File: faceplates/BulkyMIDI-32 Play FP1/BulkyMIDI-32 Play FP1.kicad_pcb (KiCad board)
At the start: 2 copper layers, 100 x 23.2 mm, 4 parts, among them M1 Mounting_Pin, M2 Mounting_Pin, M3 Mounting_Pin, M4 Mounting_Pin

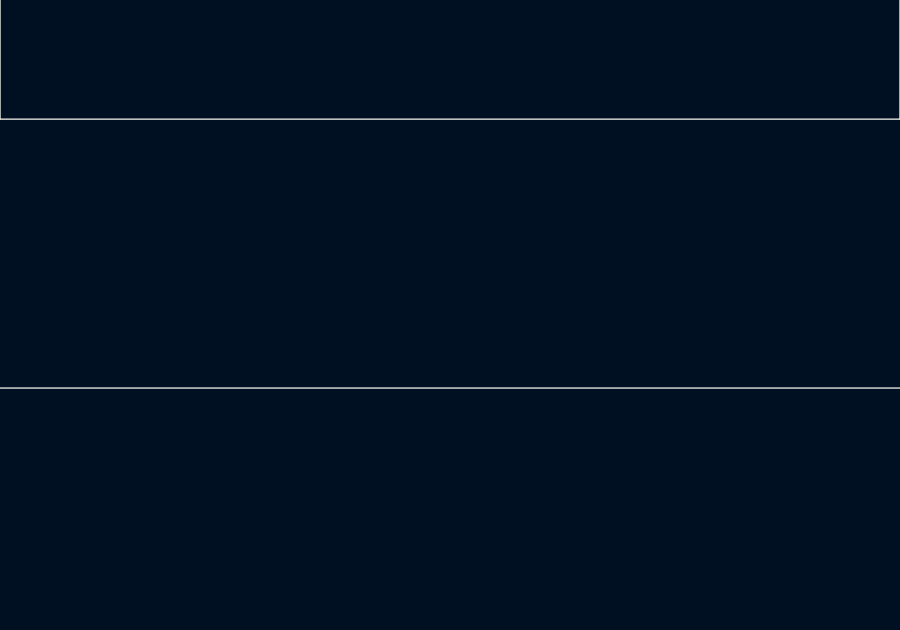
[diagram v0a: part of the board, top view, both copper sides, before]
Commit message: Channel logo added to FP1, same with Play
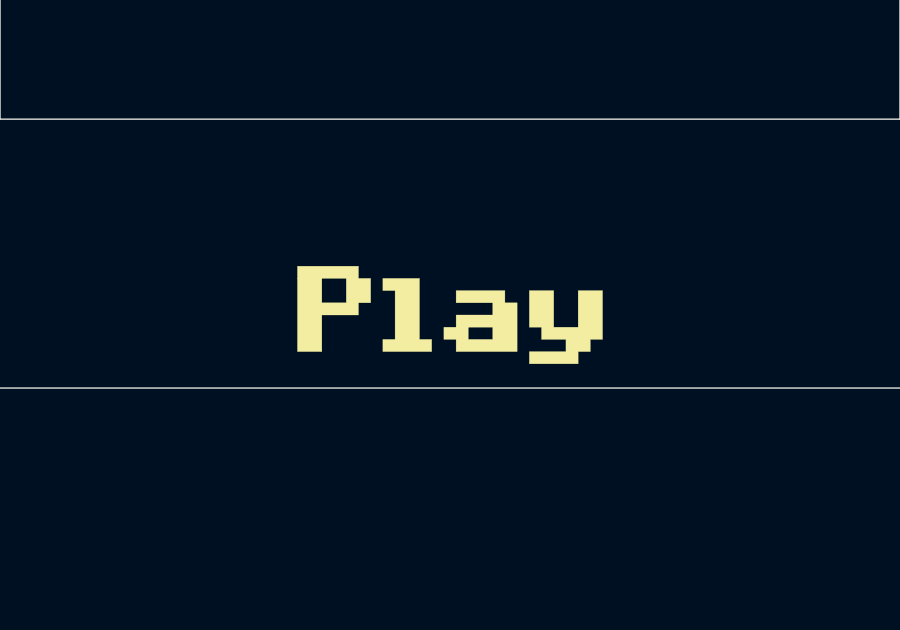
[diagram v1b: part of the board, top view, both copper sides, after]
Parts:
- added G***: LOGO, artwork:Play, F.Cu at (141.1, 131.7)
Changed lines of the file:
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@@
     (tracks 0)
     (zones 0)
-    (modules 4)
+    (modules 5)
     (nets 2)
   )
@@
     (add_net GND)
   )
+  (module artwork:Play (layer F.Cu)
+    (at 141.09 131.739)
+    (fp_text reference G*** (at 0 0) (layer F.SilkS) hide
+      (effects (font (size 1.524 1.524) (thickness 0.3)))
+    )
+    (fp_text value LOGO (at 0.75 0) (layer F.SilkS) hide
+      (effects (font (size 1.524 1.524) (thickness 0.3)))
+    )
+    (fp_poly (pts (xy 3.457857 0.406807) (xy 4.271471 0.406807) (xy 4.271471 -0.813614) (xy 5.085085 -0.813614)
+      (xy 5.085085 0.813613) (xy 4.678278 0.813613) (xy 4.678278 1.22042) (xy 4.271471 1.22042)
+      (xy 4.271471 1.627227) (xy 2.644244 1.627227) (xy 2.644244 1.22042) (xy 3.864664 1.22042)
+      (xy 3.864664 0.813613) (xy 3.051051 0.813613) (xy 3.051051 0.406807) (xy 2.644244 0.406807)
+      (xy 2.644244 -0.813614) (xy 3.457857 -0.813614) (xy 3.457857 0.406807)) (layer F.SilkS) (width 0.01))
+    (fp_poly (pts (xy -3.051051 -1.220421) (xy -2.644245 -1.220421) (xy -2.644245 -0.406807) (xy -3.051051 -0.406807)
+      (xy -3.051051 0) (xy -4.271472 0) (xy -4.271472 1.22042) (xy -5.085085 1.22042)
+      (xy -5.085085 -1.220421) (xy -4.271472 -1.220421) (xy -4.271472 -0.406807) (xy -3.457858 -0.406807)
+      (xy -3.457858 -1.220421) (xy -4.271472 -1.220421) (xy -5.085085 -1.220421) (xy -5.085085 -1.627227)
+      (xy -3.051051 -1.627227) (xy -3.051051 -1.220421)) (layer F.SilkS) (width 0.01))
+    (fp_poly (pts (xy -1.017017 0.813613) (xy -0.610211 0.813613) (xy -0.610211 1.22042) (xy -2.237438 1.22042)
+      (xy -2.237438 0.813613) (xy -1.830631 0.813613) (xy -1.830631 -0.813614) (xy -2.237438 -0.813614)
+      (xy -2.237438 -1.220421) (xy -1.017017 -1.220421) (xy -1.017017 0.813613)) (layer F.SilkS) (width 0.01))
+    (fp_poly (pts (xy 1.83063 -0.406807) (xy 2.237437 -0.406807) (xy 2.237437 1.22042) (xy 0.203403 1.22042)
+      (xy 0.203403 0.813613) (xy -0.203404 0.813613) (xy -0.203404 0.406807) (xy 0.203403 0.406807)
+      (xy 0.61021 0.406807) (xy 0.61021 0.813613) (xy 1.423823 0.813613) (xy 1.423823 0.406807)
+      (xy 0.61021 0.406807) (xy 0.203403 0.406807) (xy 0.203403 0) (xy 1.423823 0)
+      (xy 1.423823 -0.406807) (xy 0.203403 -0.406807) (xy 0.203403 -0.813614) (xy 1.83063 -0.813614)
+      (xy 1.83063 -0.406807)) (layer F.SilkS) (width 0.01))
+  )
   (module mounting:M3_pin (layer F.Cu)
     (at 99.815 129.199)
@@
       (effects (font (size 1 1) (thickness 0.15)))
     )
+    (fp_circle (center 0 0) (end 2 0.8) (layer F.Fab) (width 0.1))
     (fp_circle (center 0 0) (end 2.6 0) (layer F.CrtYd) (width 0.05))
-    (fp_circle (center 0 0) (end 2 0.8) (layer F.Fab) (width 0.1))
     (pad 1 thru_hole circle (at 0 0) (size 3.5 3.5) (drill 3.048) (layers *.Cu *.Mask)
       (net 1 GND) (solder_mask_margin 0.8))
@@
       (effects (font (size 1 1) (thickness 0.15)))
     )
+    (fp_circle (center 0 0) (end 2.6 0) (layer F.CrtYd) (width 0.05))
     (fp_circle (center 0 0) (end 2 0.8) (layer F.Fab) (width 0.1))
-    (fp_circle (center 0 0) (end 2.6 0) (layer F.CrtYd) (width 0.05))
     (pad 1 thru_hole circle (at 0 0) (size 3.5 3.5) (drill 3.048) (layers *.Cu *.Mask)
       (net 1 GND) (solder_mask_margin 0.8))
@@
       (effects (font (size 1 1) (thickness 0.15)))
     )
+    (fp_circle (center 0 0) (end 2 0.8) (layer F.Fab) (width 0.1))
     (fp_circle (center 0 0) (end 2.6 0) (layer F.CrtYd) (width 0.05))
-    (fp_circle (center 0 0) (end 2 0.8) (layer F.Fab) (width 0.1))
     (pad 1 thru_hole circle (at 0 0) (size 3.5 3.5) (drill 3.048) (layers *.Cu *.Mask)
       (net 1 GND) (solder_mask_margin 0.8))
@@
       (effects (font (size 1 1) (thickness 0.15)))
     )
+    (fp_circle (center 0 0) (end 2.6 0) (layer F.CrtYd) (width 0.05))
     (fp_circle (center 0 0) (end 2 0.8) (layer F.Fab) (width 0.1))
-    (fp_circle (center 0 0) (end 2.6 0) (layer F.CrtYd) (width 0.05))
     (pad 1 thru_hole circle (at 0 0) (size 3.5 3.5) (drill 3.048) (layers *.Cu *.Mask)
       (net 1 GND) (solder_mask_margin 0.8))

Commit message: Silkscreen logo tweak
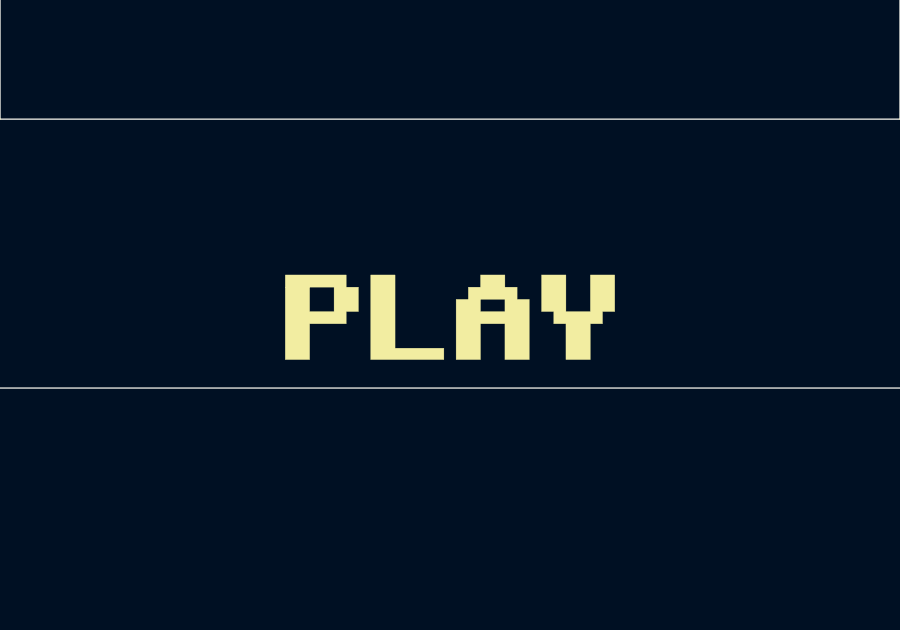
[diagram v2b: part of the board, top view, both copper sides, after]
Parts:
- moved G*** 0.06 mm to (141.1, 131.8)
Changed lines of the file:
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@@
     (add_net GND)
   )
-  (module artwork:Play (layer F.Cu)
-    (at 141.09 131.739)
+  (module artwork:Play locked (layer F.Cu)
+    (at 141.09 131.8025)
     (fp_text reference G*** (at 0 0) (layer F.SilkS) hide
       (effects (font (size 1.524 1.524) (thickness 0.3)))
@@
       (effects (font (size 1.524 1.524) (thickness 0.3)))
     )
-    (fp_poly (pts (xy 3.457857 0.406807) (xy 4.271471 0.406807) (xy 4.271471 -0.813614) (xy 5.085085 -0.813614)
-      (xy 5.085085 0.813613) (xy 4.678278 0.813613) (xy 4.678278 1.22042) (xy 4.271471 1.22042)
-      (xy 4.271471 1.627227) (xy 2.644244 1.627227) (xy 2.644244 1.22042) (xy 3.864664 1.22042)
-      (xy 3.864664 0.813613) (xy 3.051051 0.813613) (xy 3.051051 0.406807) (xy 2.644244 0.406807)
-      (xy 2.644244 -0.813614) (xy 3.457857 -0.813614) (xy 3.457857 0.406807)) (layer F.SilkS) (width 0.01))
-    (fp_poly (pts (xy -3.051051 -1.220421) (xy -2.644245 -1.220421) (xy -2.644245 -0.406807) (xy -3.051051 -0.406807)
-      (xy -3.051051 0) (xy -4.271472 0) (xy -4.271472 1.22042) (xy -5.085085 1.22042)
-      (xy -5.085085 -1.220421) (xy -4.271472 -1.220421) (xy -4.271472 -0.406807) (xy -3.457858 -0.406807)
-      (xy -3.457858 -1.220421) (xy -4.271472 -1.220421) (xy -5.085085 -1.220421) (xy -5.085085 -1.627227)
-      (xy -3.051051 -1.627227) (xy -3.051051 -1.220421)) (layer F.SilkS) (width 0.01))
-    (fp_poly (pts (xy -1.017017 0.813613) (xy -0.610211 0.813613) (xy -0.610211 1.22042) (xy -2.237438 1.22042)
-      (xy -2.237438 0.813613) (xy -1.830631 0.813613) (xy -1.830631 -0.813614) (xy -2.237438 -0.813614)
-      (xy -2.237438 -1.220421) (xy -1.017017 -1.220421) (xy -1.017017 0.813613)) (layer F.SilkS) (width 0.01))
-    (fp_poly (pts (xy 1.83063 -0.406807) (xy 2.237437 -0.406807) (xy 2.237437 1.22042) (xy 0.203403 1.22042)
-      (xy 0.203403 0.813613) (xy -0.203404 0.813613) (xy -0.203404 0.406807) (xy 0.203403 0.406807)
-      (xy 0.61021 0.406807) (xy 0.61021 0.813613) (xy 1.423823 0.813613) (xy 1.423823 0.406807)
-      (xy 0.61021 0.406807) (xy 0.203403 0.406807) (xy 0.203403 0) (xy 1.423823 0)
-      (xy 1.423823 -0.406807) (xy 0.203403 -0.406807) (xy 0.203403 -0.813614) (xy 1.83063 -0.813614)
-      (xy 1.83063 -0.406807)) (layer F.SilkS) (width 0.01))
+    (fp_poly (pts (xy -3.457857 -0.991592) (xy -3.051051 -0.991592) (xy -3.051051 -0.177978) (xy -3.457857 -0.177978)
+      (xy -3.457857 0.228829) (xy -4.678278 0.228829) (xy -4.678278 1.423824) (xy -5.491891 1.423824)
+      (xy -5.491891 -0.991592) (xy -4.678278 -0.991592) (xy -4.678278 -0.177978) (xy -3.864664 -0.177978)
+      (xy -3.864664 -0.991592) (xy -4.678278 -0.991592) (xy -5.491891 -0.991592) (xy -5.491891 -1.398398)
+      (xy -3.457857 -1.398398) (xy -3.457857 -0.991592)) (layer F.SilkS) (width 0.01))
+    (fp_poly (pts (xy -1.83063 1.042442) (xy -0.203403 1.042442) (xy -0.203403 1.423824) (xy -2.644244 1.423824)
+      (xy -2.644244 -1.398398) (xy -1.83063 -1.398398) (xy -1.83063 1.042442)) (layer F.SilkS) (width 0.01))
+    (fp_poly (pts (xy 1.830631 -0.991592) (xy 2.237438 -0.991592) (xy 2.237438 -0.584785) (xy 2.644245 -0.584785)
+      (xy 2.644245 1.423824) (xy 1.830631 1.423824) (xy 1.830631 0.228829) (xy 1.017017 0.228829)
+      (xy 1.017017 1.423824) (xy 0.203404 1.423824) (xy 0.203404 -0.584785) (xy 0.610211 -0.584785)
+      (xy 1.017017 -0.584785) (xy 1.017017 -0.177978) (xy 1.830631 -0.177978) (xy 1.830631 -0.584785)
+      (xy 1.017017 -0.584785) (xy 0.610211 -0.584785) (xy 0.610211 -0.991592) (xy 1.017017 -0.991592)
+      (xy 1.017017 -1.398398) (xy 1.830631 -1.398398) (xy 1.830631 -0.991592)) (layer F.SilkS) (width 0.01))
+    (fp_poly (pts (xy 3.864665 -0.177978) (xy 4.678279 -0.177978) (xy 4.678279 -1.398398) (xy 5.491892 -1.398398)
+      (xy 5.491892 -0.177978) (xy 5.085085 -0.177978) (xy 5.085085 0.228829) (xy 4.678279 0.228829)
+      (xy 4.678279 1.423824) (xy 3.864665 1.423824) (xy 3.864665 0.228829) (xy 3.457858 0.228829)
+      (xy 3.457858 -0.177978) (xy 3.051051 -0.177978) (xy 3.051051 -1.398398) (xy 3.864665 -1.398398)
+      (xy 3.864665 -0.177978)) (layer F.SilkS) (width 0.01))
   )
   (module mounting:M3_pin (layer F.Cu)
@@
       (effects (font (size 1 1) (thickness 0.15)))
     )
+    (fp_circle (center 0 0) (end 2.6 0) (layer F.CrtYd) (width 0.05))
     (fp_circle (center 0 0) (end 2 0.8) (layer F.Fab) (width 0.1))
-    (fp_circle (center 0 0) (end 2.6 0) (layer F.CrtYd) (width 0.05))
     (pad 1 thru_hole circle (at 0 0) (size 3.5 3.5) (drill 3.048) (layers *.Cu *.Mask)
       (net 1 GND) (solder_mask_margin 0.8))
@@
       (effects (font (size 1 1) (thickness 0.15)))
     )
+    (fp_circle (center 0 0) (end 2 0.8) (layer F.Fab) (width 0.1))
     (fp_circle (center 0 0) (end 2.6 0) (layer F.CrtYd) (width 0.05))
-    (fp_circle (center 0 0) (end 2 0.8) (layer F.Fab) (width 0.1))
     (pad 1 thru_hole circle (at 0 0) (size 3.5 3.5) (drill 3.048) (layers *.Cu *.Mask)
       (net 1 GND) (solder_mask_margin 0.8))
@@
       (effects (font (size 1 1) (thickness 0.15)))
     )
+    (fp_circle (center 0 0) (end 2.6 0) (layer F.CrtYd) (width 0.05))
     (fp_circle (center 0 0) (end 2 0.8) (layer F.Fab) (width 0.1))
-    (fp_circle (center 0 0) (end 2.6 0) (layer F.CrtYd) (width 0.05))
     (pad 1 thru_hole circle (at 0 0) (size 3.5 3.5) (drill 3.048) (layers *.Cu *.Mask)
       (net 1 GND) (solder_mask_margin 0.8))
@@
       (effects (font (size 1 1) (thickness 0.15)))
     )
+    (fp_circle (center 0 0) (end 2 0.8) (layer F.Fab) (width 0.1))
     (fp_circle (center 0 0) (end 2.6 0) (layer F.CrtYd) (width 0.05))
-    (fp_circle (center 0 0) (end 2 0.8) (layer F.Fab) (width 0.1))
     (pad 1 thru_hole circle (at 0 0) (size 3.5 3.5) (drill 3.048) (layers *.Cu *.Mask)
       (net 1 GND) (solder_mask_margin 0.8))

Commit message: Build tweaks
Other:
- outline, holes or cut-outs redrawn
- board text added: "BulkyMIDI-32 Play FP1 (rev. B) github.com/tebl"
- board text removed: "BulkyMIDI-32 Play FP1 (rev. A) github.com/tebl"
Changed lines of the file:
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@@
   (gr_line (start 156.0887 117.5912) (end 156.0887 125.2112) (layer Edge.Cuts) (width 0.05))
   (gr_line (start 126.0913 117.5912) (end 156.0887 117.5912) (layer Edge.Cuts) (width 0.05))
-  (gr_circle (center 169.792 121.579) (end 173.094 121.579) (layer Edge.Cuts) (width 0.05))
-  (gr_text "BulkyMIDI-32\nPlay FP1 (rev. A)\ngithub.com/tebl" (at 94.1 122.849 270) (layer B.SilkS)
+  (gr_circle (center 169.792 121.579) (end 173.542 121.579) (layer Edge.Cuts) (width 0.05))
+  (gr_text "BulkyMIDI-32\nPlay FP1 (rev. B)\ngithub.com/tebl" (at 94.1 122.849 270) (layer B.SilkS)
     (effects (font (size 0.8 0.8) (thickness 0.1)) (justify mirror))
   )
